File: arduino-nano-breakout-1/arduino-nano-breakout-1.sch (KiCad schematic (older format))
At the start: 10 parts, among them J1 PJ-002A, J2 Conn_01x03_Male, J4 Conn_01x08_Male

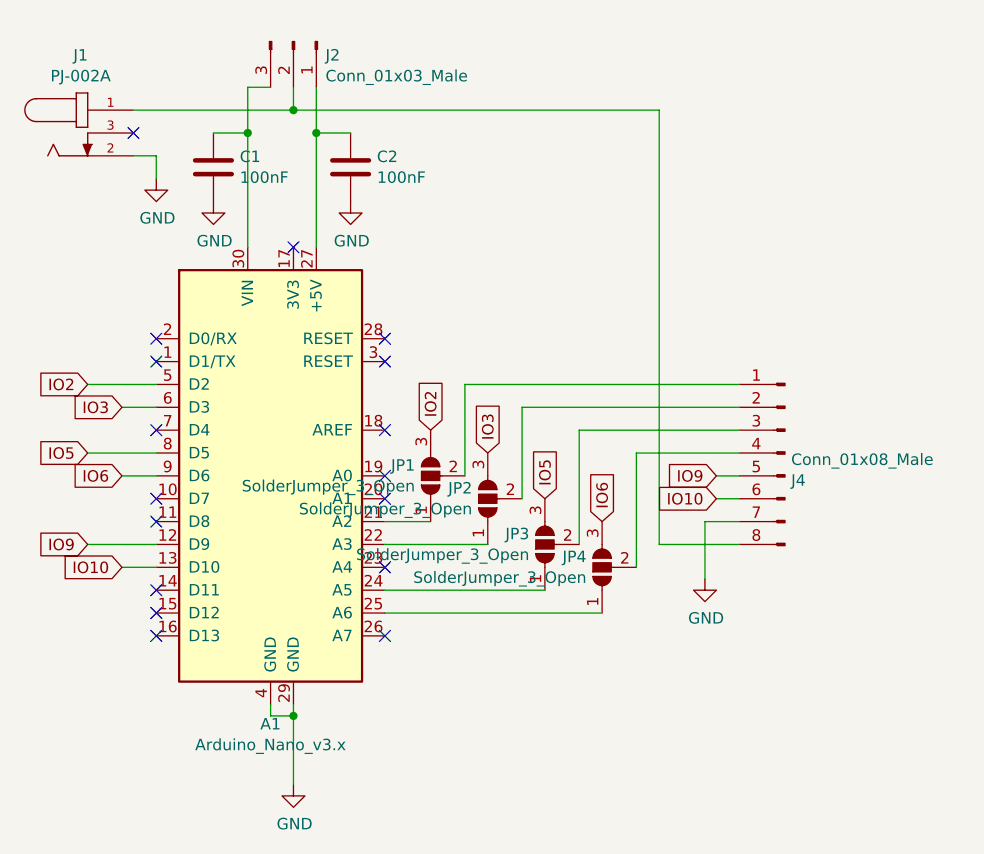
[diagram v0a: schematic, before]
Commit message: change power connector
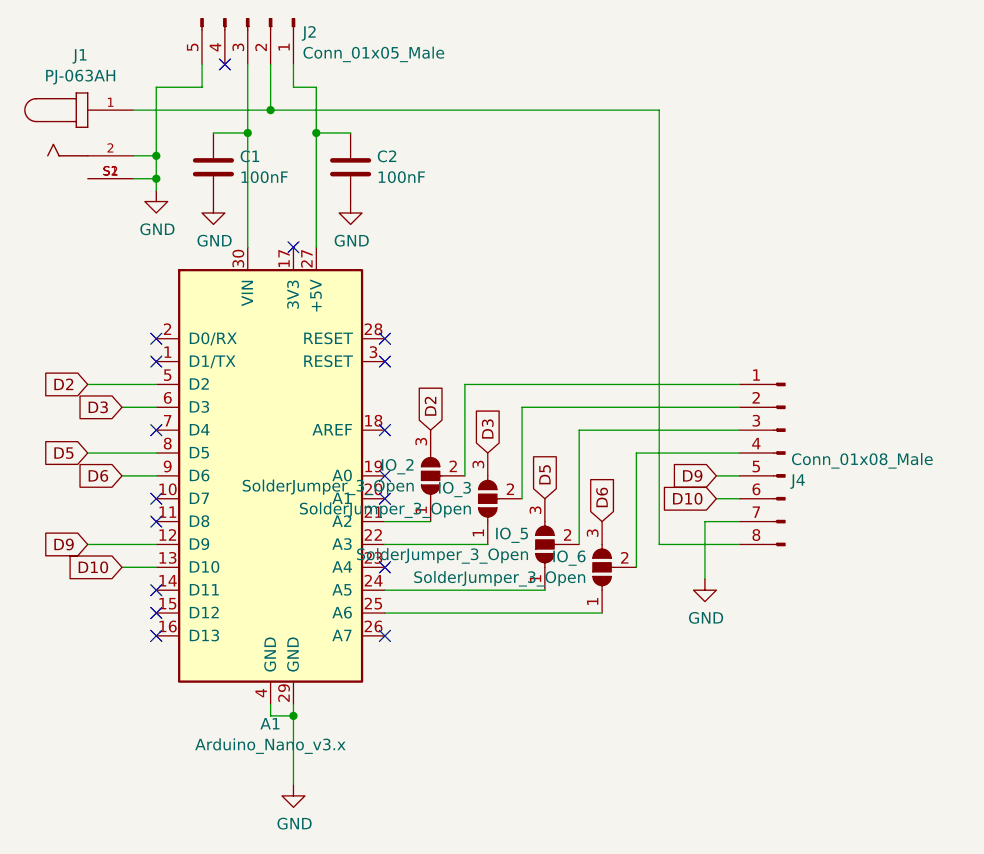
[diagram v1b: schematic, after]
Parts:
- removed J1: PJ-002A, CUI_PJ-002A, symbol SS_connectors:PJ-002A
- removed J2: Conn_01x03_Male, Connector_PinHeader_2.54mm:PinHeader_1x03_P2.54mm_Vertical, symbol Connector:Conn_01x03_Male
- added J1: PJ-063AH, CUI_PJ-063AH, symbol SS_connectors:PJ-063AH
- added J2: Conn_01x05_Male, Connector_PinHeader_2.54mm:PinHeader_1x05_P2.54mm_Vertical, symbol Connector:Conn_01x05_Male
- renumbered JP1 to IO_2, JP2 to IO_3, JP3 to IO_5, JP4 to IO_6
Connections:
- net GND: now also J1.2, J1.S1 (SHIELD), J1.S2 (SHIELD), J2.5 (Pin_5)
- net at A1.27 (+5V), C2.1: now also J2.1 (Pin_1)
- net at A1.30 (VIN), C1.1: now also J2.3 (Pin_3)
- net at J4.8 (Pin_8): now also J1.1, J2.2 (Pin_2)
- net IO10 renamed D10
- net IO2 renamed D2
- net IO3 renamed D3
- net IO5 renamed D5
- net IO6 renamed D6
- net IO9 renamed D9
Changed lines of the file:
@@
 $EndDescr
-$Comp
-L SS_connectors:PJ-002A J1
-U 1 1 5BF57EB7
-P 4250 2300
-F 0 "J1" H 4219 2640 50  0000 C CNN
-F 1 "PJ-002A" H 4219 2549 50  0000 C CNN
-F 2 "CUI_PJ-002A" H 4250 2300 50  0001 L BNN
-F 3 "https://www.digikey.fi/product-detail/en/cui-inc/PJ-002A/CP-002A-ND/96962" H 4250 2300 50  0001 L BNN
-F 4 "CUI INC" H 4250 2300 50  0001 L BNN "Field4"
-	1    4250 2300
-	1    0    0    -1
-$EndComp
-$Comp
-L Connector:Conn_01x03_Male J2
-U 1 1 5BF5969D
-P 5150 1900
-F 0 "J2" V 5210 2040 50  0000 L CNN
-F 1 "Conn_01x03_Male" V 5301 2040 50  0000 L CNN
-F 2 "Connector_PinHeader_2.54mm:PinHeader_1x03_P2.54mm_Vertical" H 5150 1900 50  0001 C CNN
-F 3 "~" H 5150 1900 50  0001 C CNN
-	1    5150 1900
-	0    1    1    0
-$EndComp
-Wire Wire Line
-	5150 2200 5150 2100
 $Comp
 L power:GND #PWR0101
@@
 L power:GND #PWR0103
 U 1 1 5BF59B46
-P 4550 2500
-F 0 "#PWR0103" H 4550 2250 50  0001 C CNN
-F 1 "GND" H 4555 2327 50  0000 C CNN
-F 2 "" H 4550 2500 50  0001 C CNN
-F 3 "" H 4550 2500 50  0001 C CNN
-	1    4550 2500
+P 4550 2550
+F 0 "#PWR0103" H 4550 2300 50  0001 C CNN
+F 1 "GND" H 4555 2377 50  0000 C CNN
+F 2 "" H 4550 2550 50  0001 C CNN
+F 3 "" H 4550 2550 50  0001 C CNN
+	1    4550 2550
 	1    0    0    -1
 $EndComp
@@
 Wire Wire Line
 	4550 2400 4550 2500
-NoConn ~ 4450 2300
-Wire Wire Line
-	5150 2200 4450 2200
 $Comp
 L Connector:Conn_01x08_Male J4
@@
 $EndComp
 Text GLabel 4250 3400 0    50   Input ~ 0
-IO2
+D2
 Wire Wire Line
 	4250 3400 4550 3400
 Text GLabel 4400 3500 0    50   Input ~ 0
-IO3
+D3
 Wire Wire Line
 	4550 3500 4400 3500
 Text GLabel 4250 3700 0    50   Input ~ 0
-IO5
+D5
 Text GLabel 4400 3800 0    50   Input ~ 0
-IO6
+D6
 Wire Wire Line
 	4250 3700 4550 3700
@@
 	4400 3800 4550 3800
 Text GLabel 4250 4100 0    50   Input ~ 0
-IO9
+D9
 Text GLabel 4400 4200 0    50   Input ~ 0
-IO10
+D10
 Wire Wire Line
 	4250 4100 4550 4100
@@
 	4400 4200 4550 4200
 Text GLabel 7000 3900 0    50   Input ~ 0
-IO10
+D10
 Text GLabel 7000 3800 0    50   Input ~ 0
-IO9
+D9
 Wire Wire Line
 	7000 3800 7100 3800
@@
 	7000 3900 7100 3900
 Text GLabel 6500 4000 1    50   Input ~ 0
-IO6
+D6
 Text GLabel 6250 3900 1    50   Input ~ 0
-IO5
+D5
 Text GLabel 6000 3700 1    50   Input ~ 0
-IO3
+D3
 Text GLabel 5750 3600 1    50   Input ~ 0
-IO2
-Wire Wire Line
-	5250 2100 5250 2300
-Connection ~ 5150 2200
+D2
 Wire Wire Line
 	6750 4100 7100 4100
@@
 	6950 4000 6950 4250
 $Comp
-L Jumper:SolderJumper_3_Open JP1
+L Jumper:SolderJumper_3_Open IO_2
 U 1 1 5BF6F90F
 P 5750 3800
-F 0 "JP1" V 5796 3868 50  0000 L CNN
+F 0 "IO_2" V 5796 3868 50  0000 L CNN
 F 1 "SolderJumper_3_Open" V 5705 3868 50  0000 L CNN
 F 2 "Jumper:SolderJumper-3_P1.3mm_Open_Pad1.0x1.5mm" H 5750 3800 50  0001 C CNN
@@
 	5900 3800 5900 3400
 $Comp
-L Jumper:SolderJumper_3_Open JP2
+L Jumper:SolderJumper_3_Open IO_3
 U 1 1 5BF73B3B
 P 6000 3900
-F 0 "JP2" V 6046 3968 50  0000 L CNN
+F 0 "IO_3" V 6046 3968 50  0000 L CNN
 F 1 "SolderJumper_3_Open" V 5955 3968 50  0000 L CNN
 F 2 "Jumper:SolderJumper-3_P1.3mm_Open_Pad1.0x1.5mm" H 6000 3900 50  0001 C CNN
@@
 	6150 3500 6150 3900
 $Comp
-L Jumper:SolderJumper_3_Open JP3
+L Jumper:SolderJumper_3_Open IO_5
 U 1 1 5BF74A7B
 P 6250 4100
-F 0 "JP3" V 6296 4168 50  0000 L CNN
+F 0 "IO_5" V 6296 4168 50  0000 L CNN
 F 1 "SolderJumper_3_Open" V 6205 4168 50  0000 L CNN
 F 2 "Jumper:SolderJumper-3_P1.3mm_Open_Pad1.0x1.5mm" H 6250 4100 50  0001 C CNN
@@
 $EndComp
 $Comp
-L Jumper:SolderJumper_3_Open JP4
+L Jumper:SolderJumper_3_Open IO_6
 U 1 1 5BF74AAB
 P 6500 4200
-F 0 "JP4" V 6546 4268 50  0000 L CNN
+F 0 "IO_6" V 6546 4268 50  0000 L CNN
 F 1 "SolderJumper_3_Open" V 6455 4268 50  0000 L CNN
 F 2 "Jumper:SolderJumper-3_P1.3mm_Open_Pad1.0x1.5mm" H 6500 4200 50  0001 C CNN
@@
 Wire Wire Line
 	6150 3500 7100 3500
-Wire Wire Line
-	5150 2200 6750 2200
 Wire Wire Line
 	6400 3600 6400 4100
@@
 	1    0    0    -1
 $EndComp
-Wire Wire Line
-	5050 2100 4950 2100
-Wire Wire Line
-	4950 2100 4950 2300
 $Comp
 L power:GND #PWR0102
@@
 Wire Wire Line
 	5400 2300 5250 2300
-Connection ~ 5250 2300
 Wire Wire Line
 	5250 2300 5250 2800
@@
 Wire Wire Line
 	4950 2300 4950 2800
+$Comp
+L SS_connectors:PJ-063AH J1
+U 1 1 5BF7FA3A
+P 4250 2300
+F 0 "J1" H 4219 2640 50  0000 C CNN
+F 1 "PJ-063AH" H 4219 2549 50  0000 C CNN
+F 2 "CUI_PJ-063AH" H 4250 2300 50  0001 L BNN
+F 3 "https://www.digikey.fi/product-detail/en/cui-inc/PJ-063AH/CP-063AH-ND/2161208" H 4250 2300 50  0001 L BNN
+F 4 "CUI INC" H 4250 2300 50  0001 L BNN "Field4"
+F 5 "1.02" H 4250 2300 50  0001 L BNN "Field5"
+	1    4250 2300
+	1    0    0    -1
+$EndComp
+Wire Wire Line
+	4450 2500 4550 2500
+Wire Wire Line
+	4550 2550 4550 2500
+Connection ~ 4550 2500
+$Comp
+L Connector:Conn_01x05_Male J2
+U 1 1 5BF82757
+P 4950 1800
+F 0 "J2" V 5010 2040 50  0000 L CNN
+F 1 "Conn_01x05_Male" V 5101 2040 50  0000 L CNN
+F 2 "Connector_PinHeader_2.54mm:PinHeader_1x05_P2.54mm_Vertical" H 4950 1800 50  0001 C CNN
+F 3 "~" H 4950 1800 50  0001 C CNN
+	1    4950 1800
+	0    1    1    0
+$EndComp
+Wire Wire Line
+	4550 2400 4550 2100
+Connection ~ 4550 2400
+Wire Wire Line
+	4950 2000 4950 2300
+Wire Wire Line
+	5050 2000 5050 2200
+Connection ~ 5050 2200
+Wire Wire Line
+	5050 2200 4450 2200
+Wire Wire Line
+	5050 2200 6750 2200
+Wire Wire Line
+	5250 2300 5250 2100
+Wire Wire Line
+	5250 2100 5150 2100
+Wire Wire Line
+	5150 2100 5150 2000
+Connection ~ 5250 2300
+Wire Wire Line
+	4550 2100 4750 2100
+Wire Wire Line
+	4750 2100 4750 2000
+NoConn ~ 4850 2000
 $EndSCHEMATC

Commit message: tweaks
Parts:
- removed J4: Conn_01x08_Male, Connector_PinHeader_2.54mm:PinHeader_1x08_P2.54mm_Vertical, symbol Connector:Conn_01x08_Male
- added J3: Conn_01x10_Male, Connector_PinHeader_2.54mm:PinHeader_1x10_P2.54mm_Vertical, symbol Connector:Conn_01x10_Male
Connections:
- net D10: now also J3.3 (Pin_3)
- net D9: now also J3.4 (Pin_4)
- net GND: now also J2.1 (Pin_1), J3.2 (Pin_2); no longer J2.5 (Pin_5)
- net D1: now reaches A1.1 (D1/TX)
- net D1: now also J3.9 (Pin_9)
- net D0: now reaches A1.2 (D0/RX)
- net D0: now also J3.10 (Pin_10)
- net at A1.27 (+5V), C2.1: now also J2.5 (Pin_5); no longer J2.1 (Pin_1)
- net at IO_2.2 (C): now also J3.8 (Pin_8)
- net at IO_3.2 (C): now also J3.7 (Pin_7)
- net at IO_5.2 (C): now also J3.6 (Pin_6)
- net at IO_6.2 (C): now also J3.5 (Pin_5)
- net at J1.1: now also J2.4 (Pin_4), J3.1 (Pin_1); no longer J2.2 (Pin_2)
- no-connect marks 17 -> 15
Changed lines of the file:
@@
 encoding utf-8
 Sheet 1 1
-Title ""
-Date ""
+Title "Arduino Mini Breakout"
+Date "2018-11-23"
 Rev ""
 Comp ""
@@
 Wire Wire Line
 	4550 2400 4550 2500
-$Comp
-L Connector:Conn_01x08_Male J4
-U 1 1 5BF5B051
-P 7300 3700
-F 0 "J4" H 7273 3580 50  0000 R CNN
-F 1 "Conn_01x08_Male" H 7273 3671 50  0000 R CNN
-F 2 "Connector_PinHeader_2.54mm:PinHeader_1x08_P2.54mm_Vertical" H 7300 3700 50  0001 C CNN
-F 3 "~" H 7300 3700 50  0001 C CNN
-	1    7300 3700
-	-1   0    0    -1
-$EndComp
-Text GLabel 4250 3400 0    50   Input ~ 0
+Text GLabel 4400 3400 0    50   Input ~ 0
 D2
-Wire Wire Line
-	4250 3400 4550 3400
 Text GLabel 4400 3500 0    50   Input ~ 0
 D3
 Wire Wire Line
 	4550 3500 4400 3500
-Text GLabel 4250 3700 0    50   Input ~ 0
+Text GLabel 4400 3700 0    50   Input ~ 0
 D5
 Text GLabel 4400 3800 0    50   Input ~ 0
 D6
 Wire Wire Line
-	4250 3700 4550 3700
-Wire Wire Line
 	4400 3800 4550 3800
-Text GLabel 4250 4100 0    50   Input ~ 0
+Text GLabel 4400 4100 0    50   Input ~ 0
 D9
 Text GLabel 4400 4200 0    50   Input ~ 0
 D10
-Wire Wire Line
-	4250 4100 4550 4100
 Wire Wire Line
 	4400 4200 4550 4200
@@
 Wire Wire Line
 	6650 3700 7100 3700
-$Comp
-L MCU_Module:Arduino_Nano_v3.x A1
-U 1 1 5BF57DB9
-P 5050 3800
-F 0 "A1" H 5050 2714 50  0000 C CNN
-F 1 "Arduino_Nano_v3.x" H 5050 2623 50  0000 C CNN
-F 2 "Module:Arduino_Nano" H 5200 2850 50  0001 L CNN
-F 3 "http://www.mouser.com/pdfdocs/Gravitech_Arduino_Nano3_0.pdf" H 5050 2800 50  0001 C CNN
-	1    5050 3800
-	1    0    0    -1
-$EndComp
-NoConn ~ 4550 3200
-NoConn ~ 4550 3300
 NoConn ~ 4550 3600
 NoConn ~ 4550 3900
@@
 F 3 "~" H 4950 1800 50  0001 C CNN
 	1    4950 1800
-	0    1    1    0
+	0    -1   1    0
 $EndComp
 Wire Wire Line
@@
 	4750 2100 4750 2000
 NoConn ~ 4850 2000
+$Comp
+L Connector:Conn_01x10_Male J3
+U 1 1 5BF89C91
+P 7300 3700
+F 0 "J3" H 7273 3580 50  0000 R CNN
+F 1 "Conn_01x10_Male" H 7273 3671 50  0000 R CNN
+F 2 "Connector_PinHeader_2.54mm:PinHeader_1x10_P2.54mm_Vertical" H 7300 3700 50  0001 C CNN
+F 3 "~" H 7300 3700 50  0001 C CNN
+	1    7300 3700
+	-1   0    0    1
+$EndComp
+$Comp
+L MCU_Module:Arduino_Nano_v3.x A1
+U 1 1 5BF57DB9
+P 5050 3800
+F 0 "A1" H 5050 2714 50  0000 C CNN
+F 1 "Arduino_Nano_v3.x" H 5050 2623 50  0000 C CNN
+F 2 "Module:Arduino_Nano" H 5200 2850 50  0001 L CNN
+F 3 "http://www.mouser.com/pdfdocs/Gravitech_Arduino_Nano3_0.pdf" H 5050 2800 50  0001 C CNN
+	1    5050 3800
+	1    0    0    -1
+$EndComp
+Text GLabel 4400 3200 0    50   Input ~ 0
+D0
+Text GLabel 4400 3300 0    50   Input ~ 0
+D1
+Wire Wire Line
+	4400 3200 4550 3200
+Wire Wire Line
+	4400 3300 4550 3300
+Wire Wire Line
+	4400 3400 4550 3400
+Wire Wire Line
+	4400 3700 4550 3700
+Wire Wire Line
+	4400 4100 4550 4100
+Text GLabel 7000 3200 0    50   Input ~ 0
+D0
+Text GLabel 7000 3300 0    50   Input ~ 0
+D1
+Wire Wire Line
+	7000 3200 7100 3200
+Wire Wire Line
+	7100 3300 7000 3300
 $EndSCHEMATC

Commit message: tweak
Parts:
- J1: footprint CUI_PJ-063AH -> SS_connectors:CUI_PJ-063AH-1
- renumbered IO_2 to IO2, IO_3 to IO3, IO_5 to IO5, IO_6 to IO6
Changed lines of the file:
@@
 	6950 4000 6950 4250
 $Comp
-L Jumper:SolderJumper_3_Open IO_2
+L Jumper:SolderJumper_3_Open IO2
 U 1 1 5BF6F90F
 P 5750 3800
-F 0 "IO_2" V 5796 3868 50  0000 L CNN
+F 0 "IO2" V 5796 3868 50  0000 L CNN
 F 1 "SolderJumper_3_Open" V 5705 3868 50  0000 L CNN
 F 2 "Jumper:SolderJumper-3_P1.3mm_Open_Pad1.0x1.5mm" H 5750 3800 50  0001 C CNN
@@
 	5900 3800 5900 3400
 $Comp
-L Jumper:SolderJumper_3_Open IO_3
+L Jumper:SolderJumper_3_Open IO3
 U 1 1 5BF73B3B
 P 6000 3900
-F 0 "IO_3" V 6046 3968 50  0000 L CNN
+F 0 "IO3" V 6046 3968 50  0000 L CNN
 F 1 "SolderJumper_3_Open" V 5955 3968 50  0000 L CNN
 F 2 "Jumper:SolderJumper-3_P1.3mm_Open_Pad1.0x1.5mm" H 6000 3900 50  0001 C CNN
@@
 	6150 3500 6150 3900
 $Comp
-L Jumper:SolderJumper_3_Open IO_5
+L Jumper:SolderJumper_3_Open IO5
 U 1 1 5BF74A7B
 P 6250 4100
-F 0 "IO_5" V 6296 4168 50  0000 L CNN
+F 0 "IO5" V 6296 4168 50  0000 L CNN
 F 1 "SolderJumper_3_Open" V 6205 4168 50  0000 L CNN
 F 2 "Jumper:SolderJumper-3_P1.3mm_Open_Pad1.0x1.5mm" H 6250 4100 50  0001 C CNN
@@
 $EndComp
 $Comp
-L Jumper:SolderJumper_3_Open IO_6
+L Jumper:SolderJumper_3_Open IO6
 U 1 1 5BF74AAB
 P 6500 4200
-F 0 "IO_6" V 6546 4268 50  0000 L CNN
+F 0 "IO6" V 6546 4268 50  0000 L CNN
 F 1 "SolderJumper_3_Open" V 6455 4268 50  0000 L CNN
 F 2 "Jumper:SolderJumper-3_P1.3mm_Open_Pad1.0x1.5mm" H 6500 4200 50  0001 C CNN
@@
 L power:GND #PWR0102
 U 1 1 5BF6DF10
-P 4800 2600
-F 0 "#PWR0102" H 4800 2350 50  0001 C CNN
-F 1 "GND" H 4805 2427 50  0000 C CNN
-F 2 "" H 4800 2600 50  0001 C CNN
-F 3 "" H 4800 2600 50  0001 C CNN
-	1    4800 2600
+P 4800 2650
+F 0 "#PWR0102" H 4800 2400 50  0001 C CNN
+F 1 "GND" H 4805 2477 50  0000 C CNN
+F 2 "" H 4800 2650 50  0001 C CNN
+F 3 "" H 4800 2650 50  0001 C CNN
+	1    4800 2650
 	1    0    0    -1
 $EndComp
@@
 L power:GND #PWR0105
 U 1 1 5BF6DF2F
-P 5400 2600
-F 0 "#PWR0105" H 5400 2350 50  0001 C CNN
-F 1 "GND" H 5405 2427 50  0000 C CNN
-F 2 "" H 5400 2600 50  0001 C CNN
-F 3 "" H 5400 2600 50  0001 C CNN
-	1    5400 2600
+P 5400 2650
+F 0 "#PWR0105" H 5400 2400 50  0001 C CNN
+F 1 "GND" H 5405 2477 50  0000 C CNN
+F 2 "" H 5400 2650 50  0001 C CNN
+F 3 "" H 5400 2650 50  0001 C CNN
+	1    5400 2650
 	1    0    0    -1
 $EndComp
@@
 F 0 "J1" H 4219 2640 50  0000 C CNN
 F 1 "PJ-063AH" H 4219 2549 50  0000 C CNN
-F 2 "CUI_PJ-063AH" H 4250 2300 50  0001 L BNN
+F 2 "SS_connectors:CUI_PJ-063AH-1" H 4250 2300 50  0001 L BNN
 F 3 "https://www.digikey.fi/product-detail/en/cui-inc/PJ-063AH/CP-063AH-ND/2161208" H 4250 2300 50  0001 L BNN
 F 4 "CUI INC" H 4250 2300 50  0001 L BNN "Field4"
@@
 Wire Wire Line
 	7100 3300 7000 3300
+Wire Wire Line
+	5400 2600 5400 2650
+Wire Wire Line
+	4800 2600 4800 2650
 $EndSCHEMATC
